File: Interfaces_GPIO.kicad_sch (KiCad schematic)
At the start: 8 parts

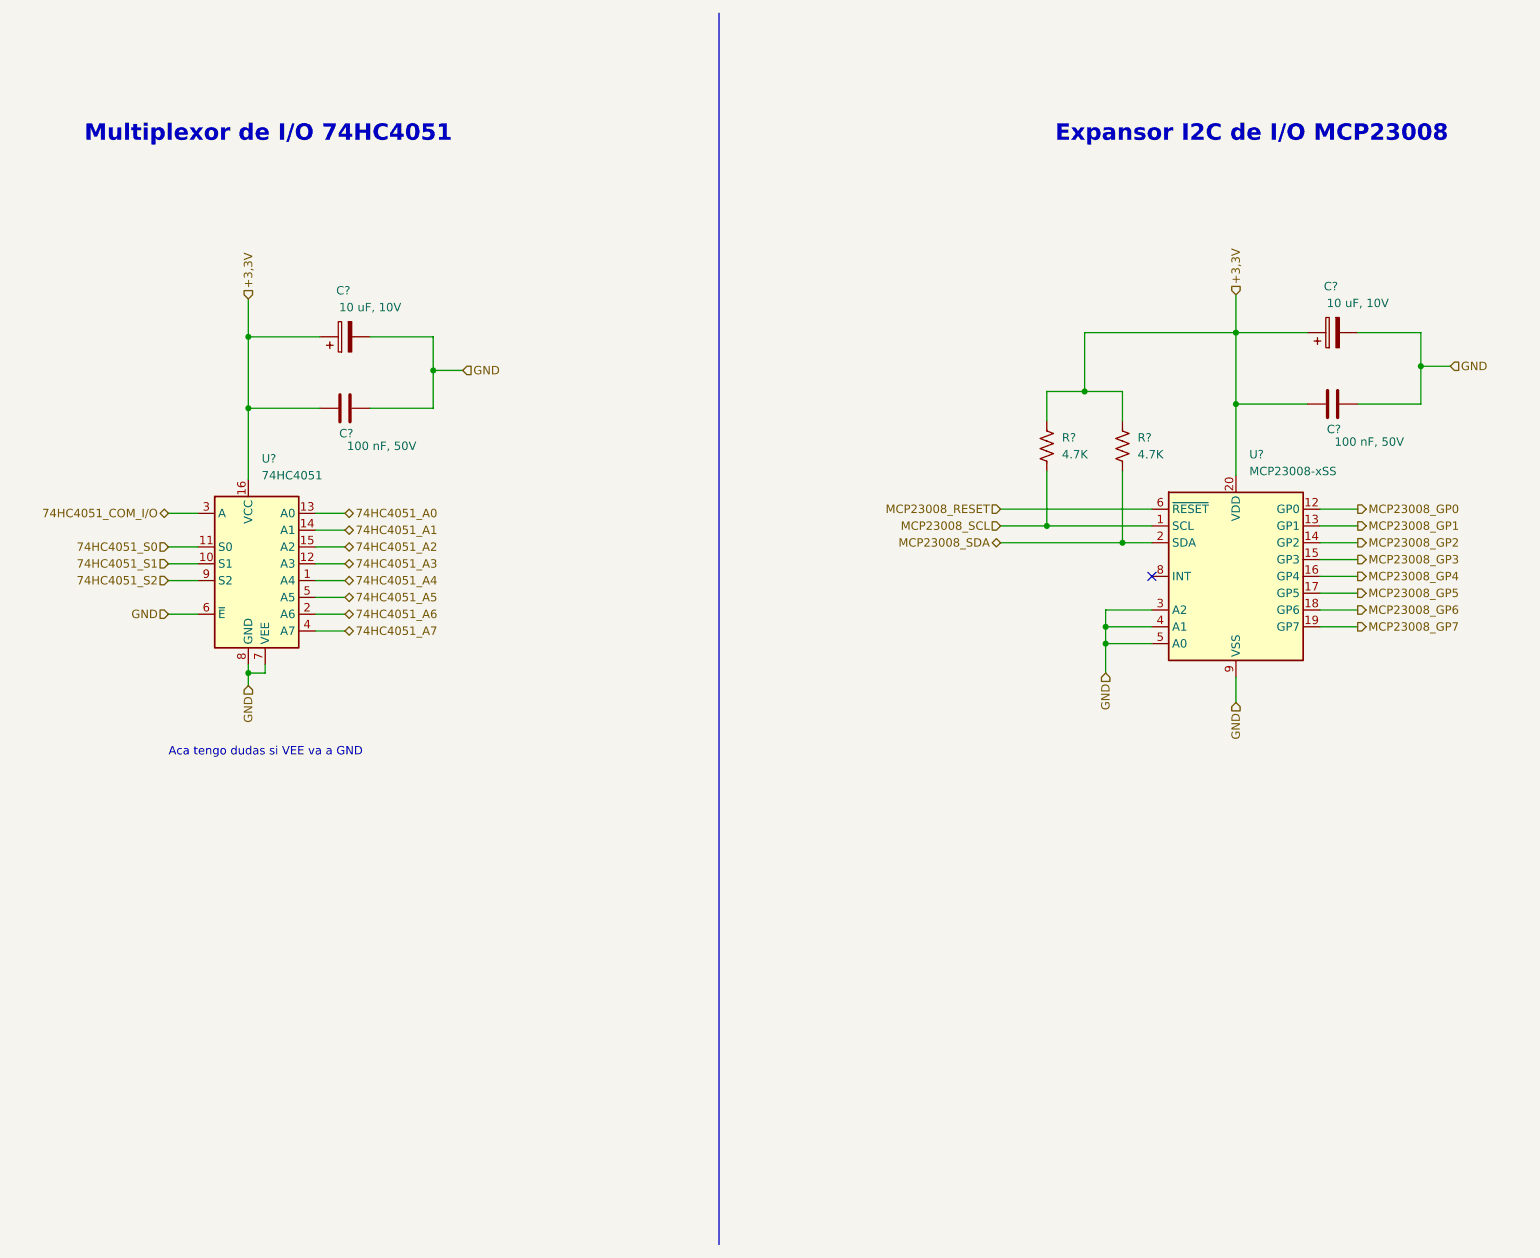
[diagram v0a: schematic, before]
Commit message: Ajuste del esquematico
Se cambio el integrado ESP32 por 2 tiras de pines de 1x15, se quitaron los switches EN y BOOT que ya estan en el NodeMCU, se quito el mutliplexor 74HC y se cablearon las I/O
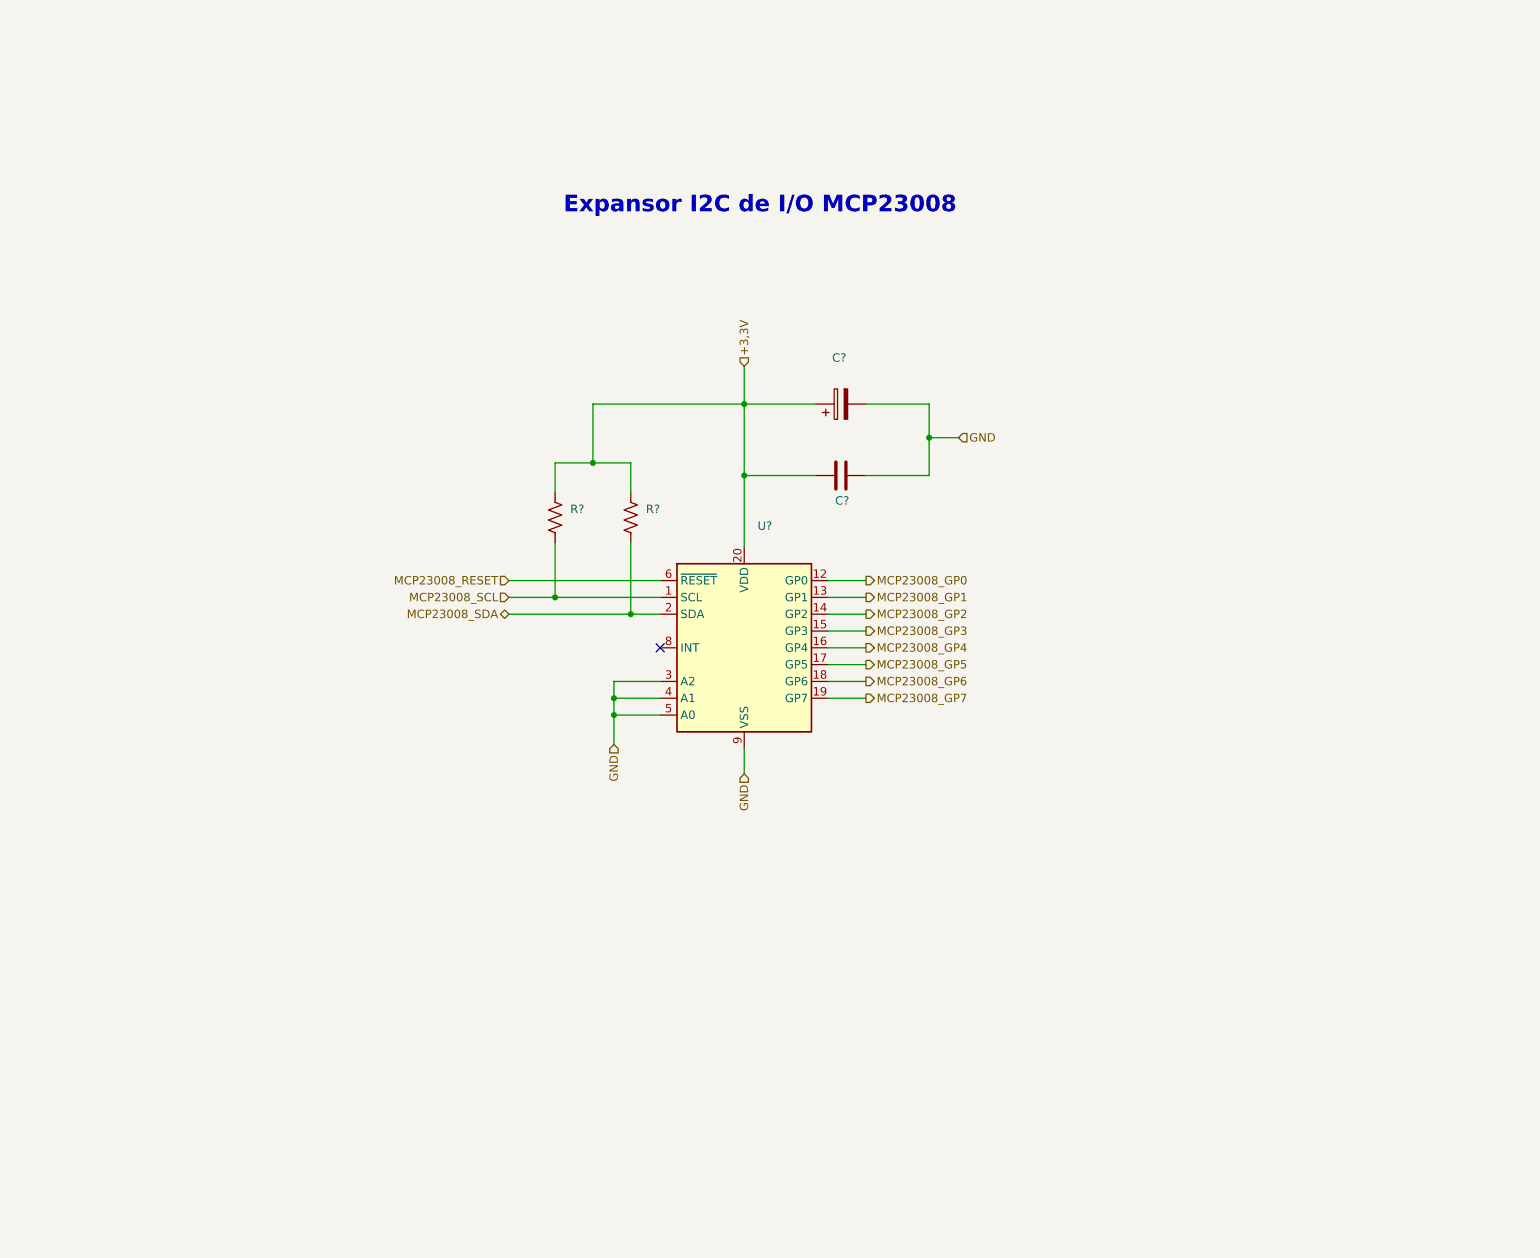
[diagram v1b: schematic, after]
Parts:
- removed C?: 100 nF, 50V, symbol Device:C
- removed C?: 10 uF, 10V, symbol Device:C_Polarized
- removed U?: 74HC4051, Package_SO:SOIC-16_3.9x9.9mm_P1.27mm, symbol 74xx:74HC4051
- C?: value 100 nF, 50V -> (none)
- C?: value 10 uF, 10V -> (none)
- R? (x2): value 4.7K -> (none)
- U?: value MCP23008-xSS -> (none); footprint Package_SO:SSOP-20_5.3x7.2mm_P0.65mm -> (none)
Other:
- note removed: "Aca tengo dudas si VEE va a GND"
- note removed: "Multiplexor de I/O 74HC4051"
- moved on the sheet: C?, R?, U?

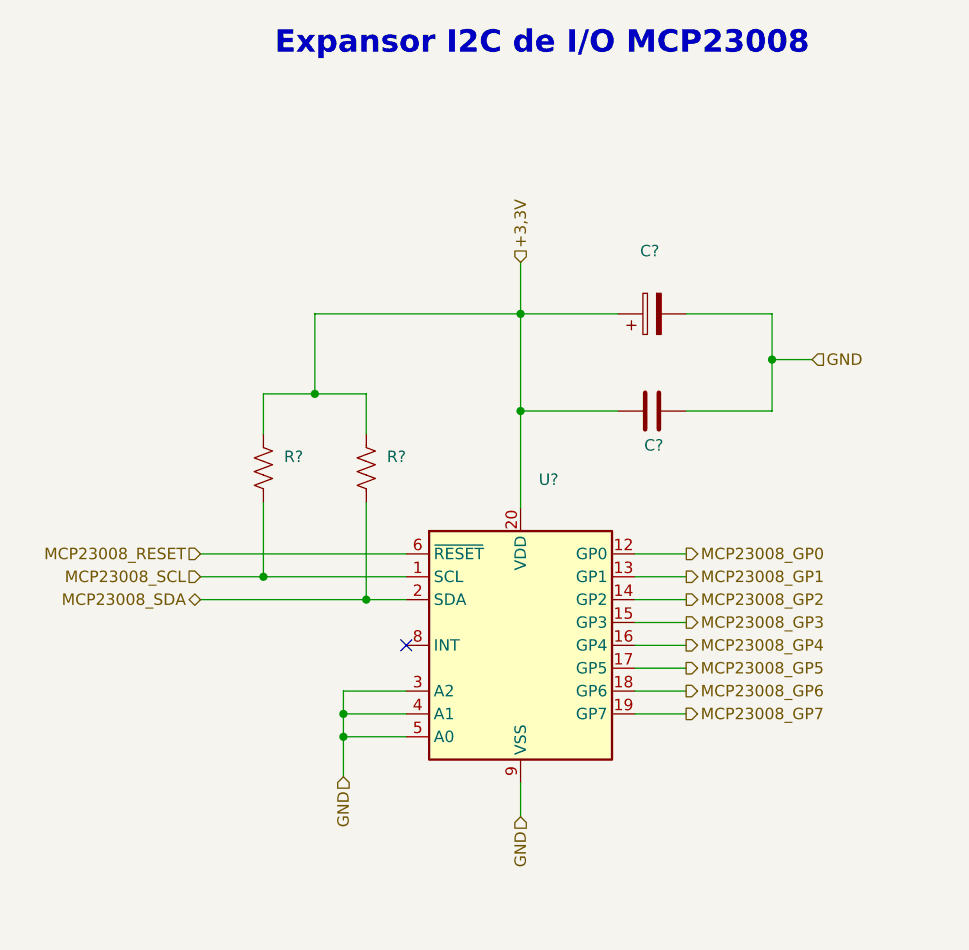
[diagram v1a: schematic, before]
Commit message: Modificación de posición de circ. filtrado y circ. de adaptación de tensión
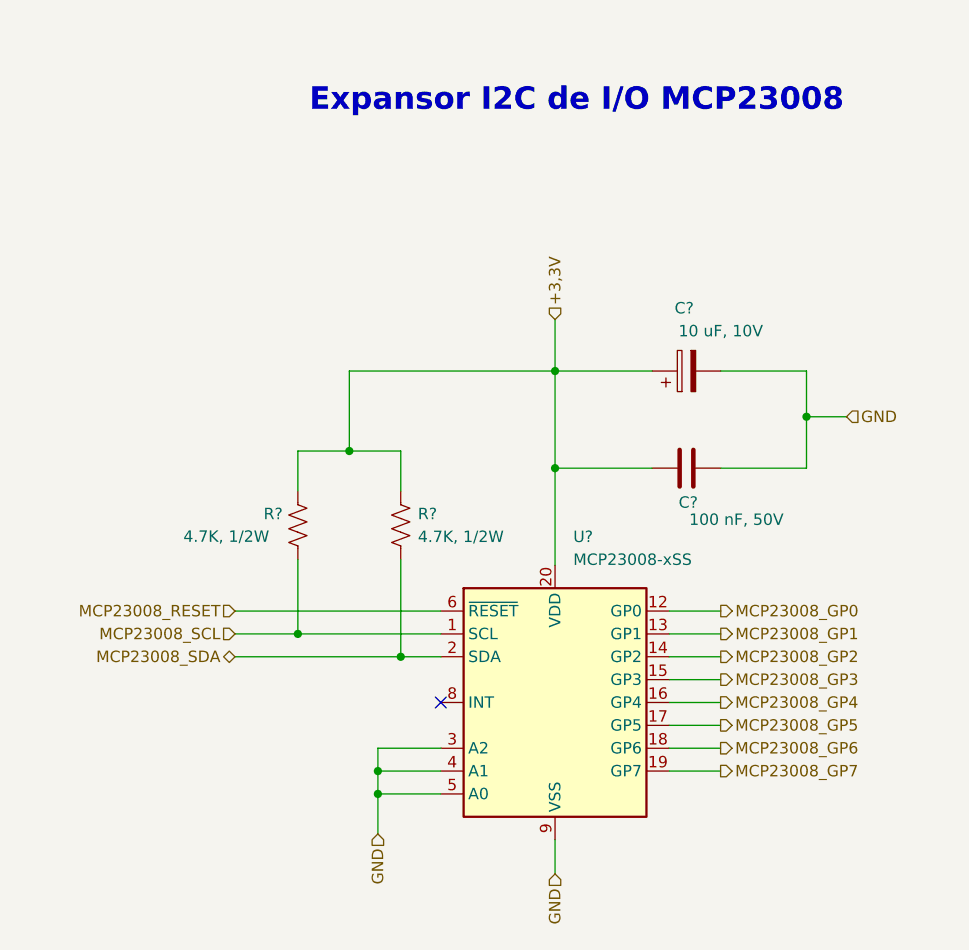
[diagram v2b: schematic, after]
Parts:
- C?: value (none) -> 100 nF, 50V
- C?: value (none) -> 10 uF, 10V
- R? (x2): value (none) -> 4.7K, 1/2W
- U?: value (none) -> MCP23008-xSS; footprint (none) -> Package_SO:SSOP-20_5.3x7.2mm_P0.65mm
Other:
- moved on the sheet: C?, R?, U?

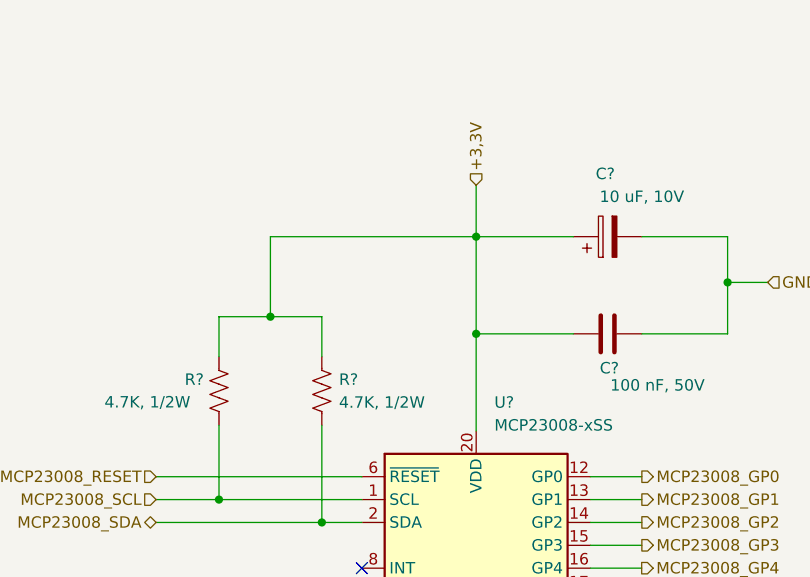
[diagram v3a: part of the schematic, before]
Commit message: Actualización de SCH según placa industrial, y búsqueda de footprints.
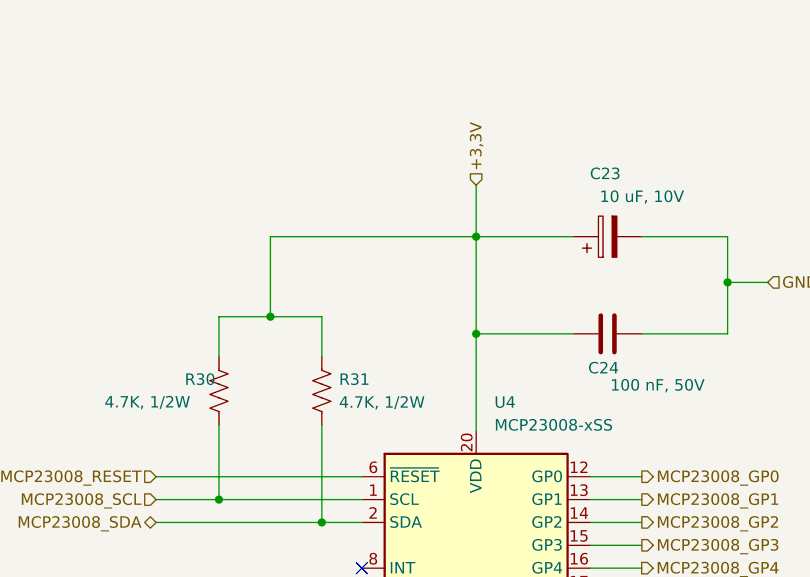
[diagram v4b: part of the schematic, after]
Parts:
- C23, C24: renamed from C?; footprint (none) -> Capacitor_SMD:C_0805_2012Metric
- R30, R31: renamed from R?; footprint (none) -> Resistor_SMD:R_0805_2012Metric
- gave numbers to parts that had none: 1
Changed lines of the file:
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@@
   (symbol (lib_id "Device:C") (at 162.5803 88.265 90) (unit 1)
     (in_bom yes) (on_board yes)
-    (property "Reference" "C?" (id 0) (at 163.8503 92.075 90)
+    (property "Reference" "C24" (id 0) (at 163.8503 92.075 90)
       (effects (font (size 1.27 1.27)) (justify left))
     )
@@
       (effects (font (size 1.27 1.27)) (justify left))
     )
-    (property "Footprint" "" (id 2) (at 166.3903 87.2998 0)
+    (property "Footprint" "Capacitor_SMD:C_0805_2012Metric" (id 2) (at 166.3903 87.2998 0)
       (effects (font (size 1.27 1.27)) hide)
     )
@@
   (symbol (lib_id "Device:R_US") (at 130.8303 94.615 0) (unit 1)
     (in_bom yes) (on_board yes) (fields_autoplaced)
-    (property "Reference" "R?" (id 0) (at 132.7353 93.3449 0)
+    (property "Reference" "R31" (id 0) (at 132.7353 93.3449 0)
       (effects (font (size 1.27 1.27)) (justify left))
     )
@@
       (effects (font (size 1.27 1.27)) (justify left))
     )
-    (property "Footprint" "" (id 2) (at 131.8463 94.869 90)
+    (property "Footprint" "Resistor_SMD:R_0805_2012Metric" (id 2) (at 131.8463 94.869 90)
       (effects (font (size 1.27 1.27)) hide)
     )
@@
   (symbol (lib_id "Device:C_Polarized") (at 162.5803 77.47 90) (unit 1)
     (in_bom yes) (on_board yes)
-    (property "Reference" "C?" (id 0) (at 162.3263 70.485 90))
+    (property "Reference" "C23" (id 0) (at 162.3263 70.485 90))
     (property "Value" "10 uF, 10V" (id 1) (at 166.3903 73.025 90))
-    (property "Footprint" "" (id 2) (at 166.3903 76.5048 0)
+    (property "Footprint" "Capacitor_SMD:C_0805_2012Metric" (id 2) (at 166.3903 76.5048 0)
       (effects (font (size 1.27 1.27)) hide)
     )
@@
   (symbol (lib_id "Device:R_US") (at 119.4003 94.615 0) (unit 1)
     (in_bom yes) (on_board yes)
-    (property "Reference" "R?" (id 0) (at 115.5903 93.345 0)
+    (property "Reference" "R30" (id 0) (at 115.5903 93.345 0)
       (effects (font (size 1.27 1.27)) (justify left))
     )
@@
       (effects (font (size 1.27 1.27)) (justify left))
     )
-    (property "Footprint" "" (id 2) (at 120.4163 94.869 90)
+    (property "Footprint" "Resistor_SMD:R_0805_2012Metric" (id 2) (at 120.4163 94.869 90)
       (effects (font (size 1.27 1.27)) hide)
     )
@@
   (symbol (lib_id "Interface_Expansion:MCP23008-xSS") (at 147.9753 114.3 0) (unit 1)
     (in_bom yes) (on_board yes) (fields_autoplaced)
-    (property "Reference" "U?" (id 0) (at 149.9947 95.885 0)
+    (property "Reference" "U4" (id 0) (at 149.9947 95.885 0)
       (effects (font (size 1.27 1.27)) (justify left))
     )

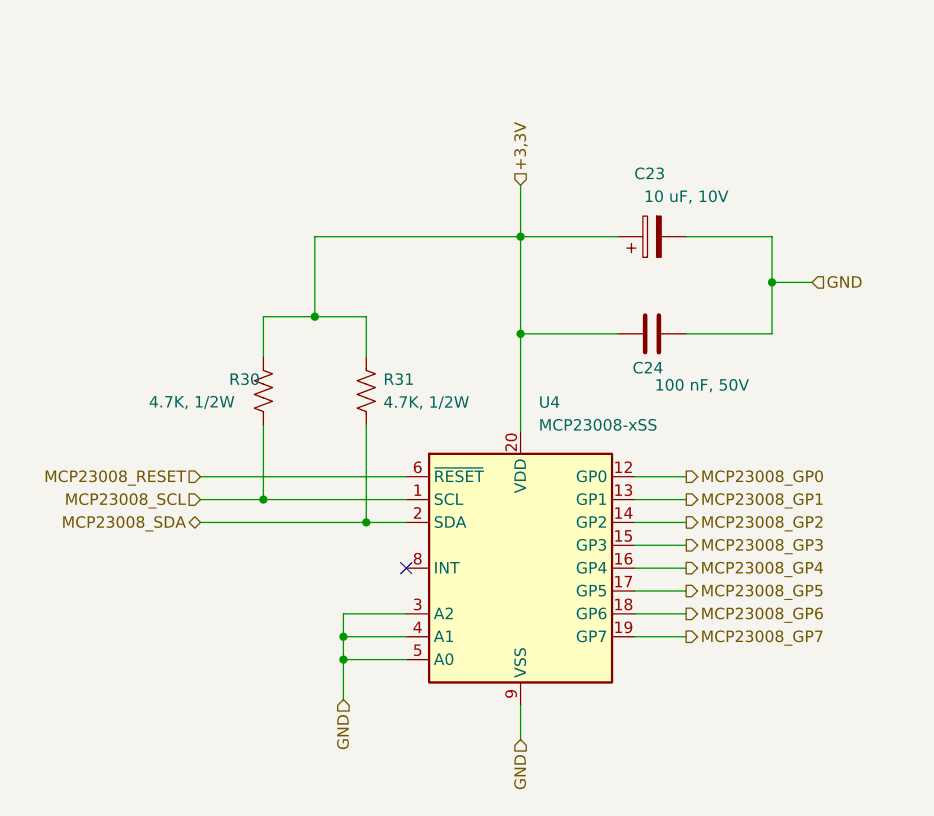
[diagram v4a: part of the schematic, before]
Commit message: Cambios en SCH y PCB.
Se cambio el adaptador de nivel 5-3,3V por un circuito con MOSFET 2N7002, dado que ya no hay stock del NXB. Se modificó el footprint del expansor I/O por uno thorugh-hole.
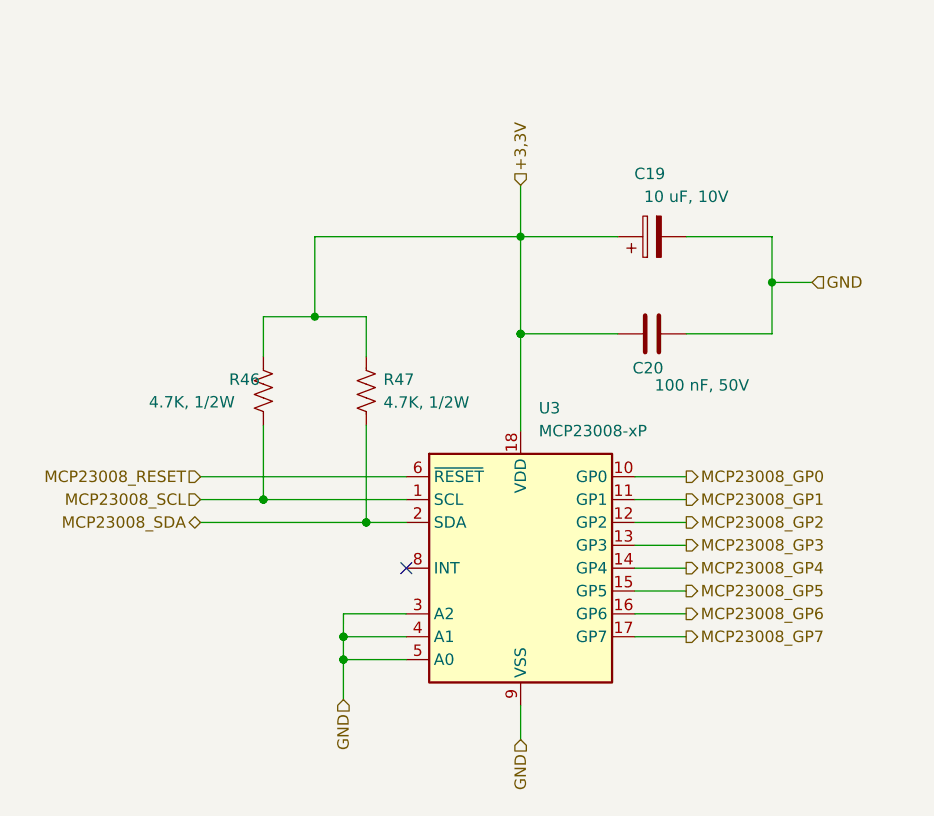
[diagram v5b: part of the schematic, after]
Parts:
- removed U4: MCP23008-xSS, Package_SO:SSOP-20_5.3x7.2mm_P0.65mm, symbol Interface_Expansion:MCP23008-xSS
- added U3: MCP23008-xP, Package_DIP:DIP-18_W7.62mm, symbol Interface_Expansion:MCP23008-xP
- renumbered C23 to C19, C24 to C20, R30 to R46, R31 to R47
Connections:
- net +3,3V: now also U3.18 (VDD)
- net GND: now also U3.3 (A2), U3.4 (A1), U3.5 (A0), U3.9 (VSS)
- net MCP23008_GP0: now also U3.10 (GP0)
- net MCP23008_GP1: now also U3.11 (GP1)
- net MCP23008_GP2: now also U3.12 (GP2)
- net MCP23008_GP3: now also U3.13 (GP3)
- net MCP23008_GP4: now also U3.14 (GP4)
- net MCP23008_GP5: now also U3.15 (GP5)
- net MCP23008_GP6: now also U3.16 (GP6)
- net MCP23008_GP7: now also U3.17 (GP7)
- net MCP23008_RESET: now also U3.6 (~{RESET})
- net MCP23008_SCL: now also U3.1 (SCL)
- net MCP23008_SDA: now also U3.2 (SDA)
